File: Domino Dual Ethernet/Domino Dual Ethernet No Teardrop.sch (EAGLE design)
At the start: 37 parts, among them J1 HL-59T-2X1, J2 MH18-1, J3 MH18-1

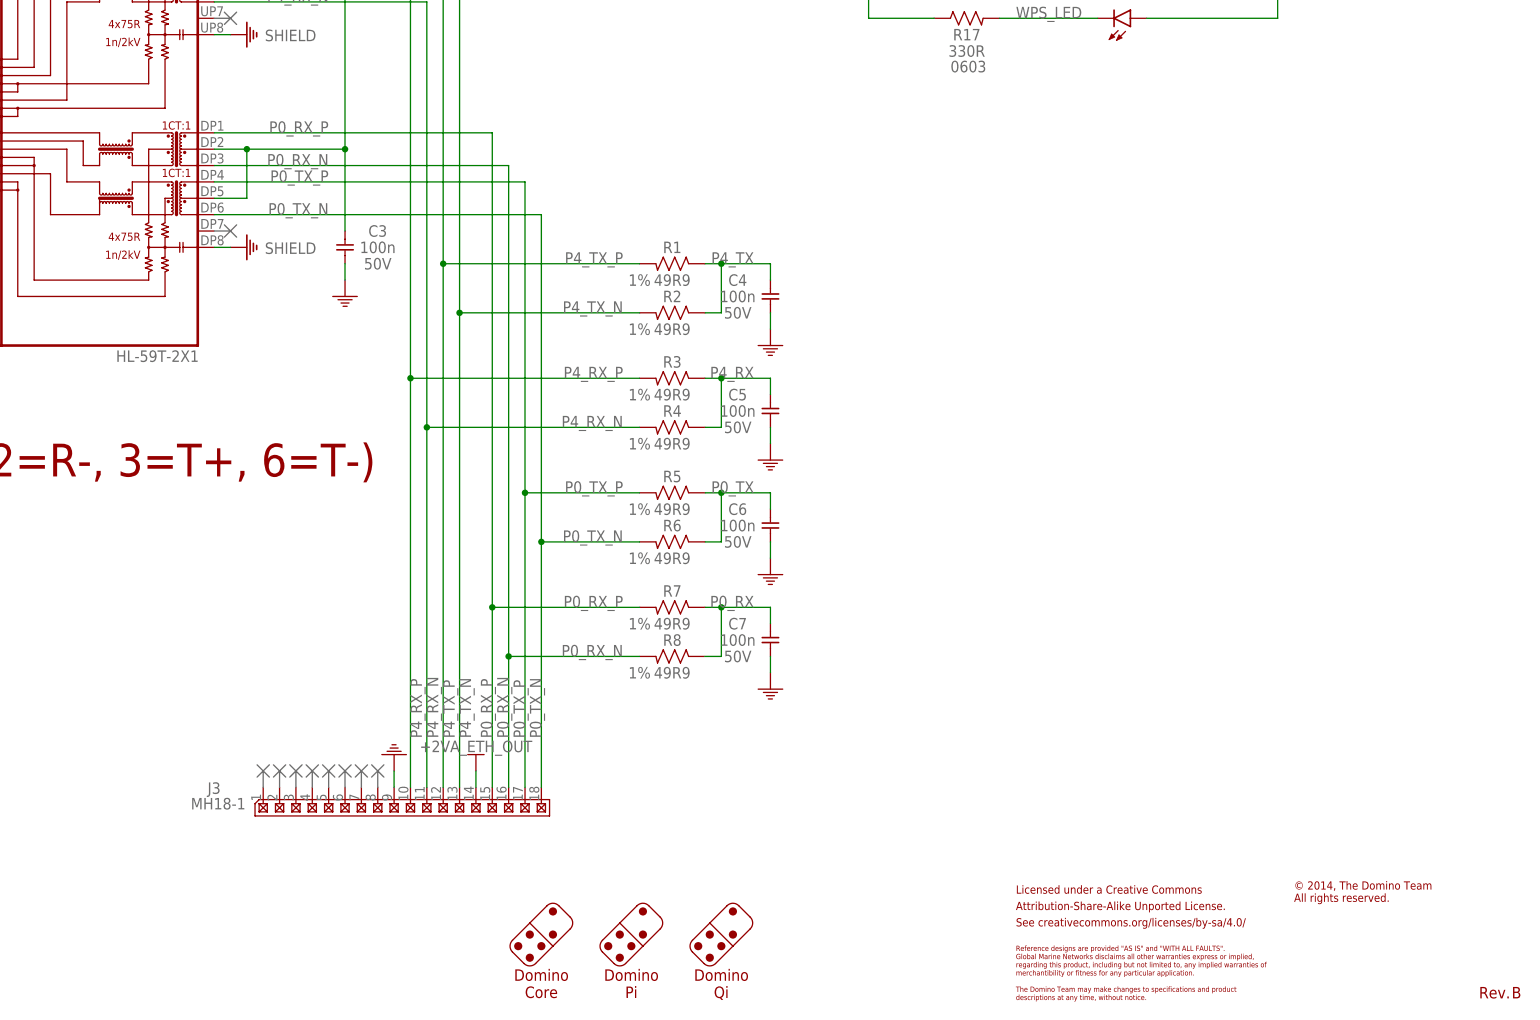
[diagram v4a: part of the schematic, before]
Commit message: Domino Dual Ethernet Rev. C: Changed dual Magjack connector for new one, changed Logos
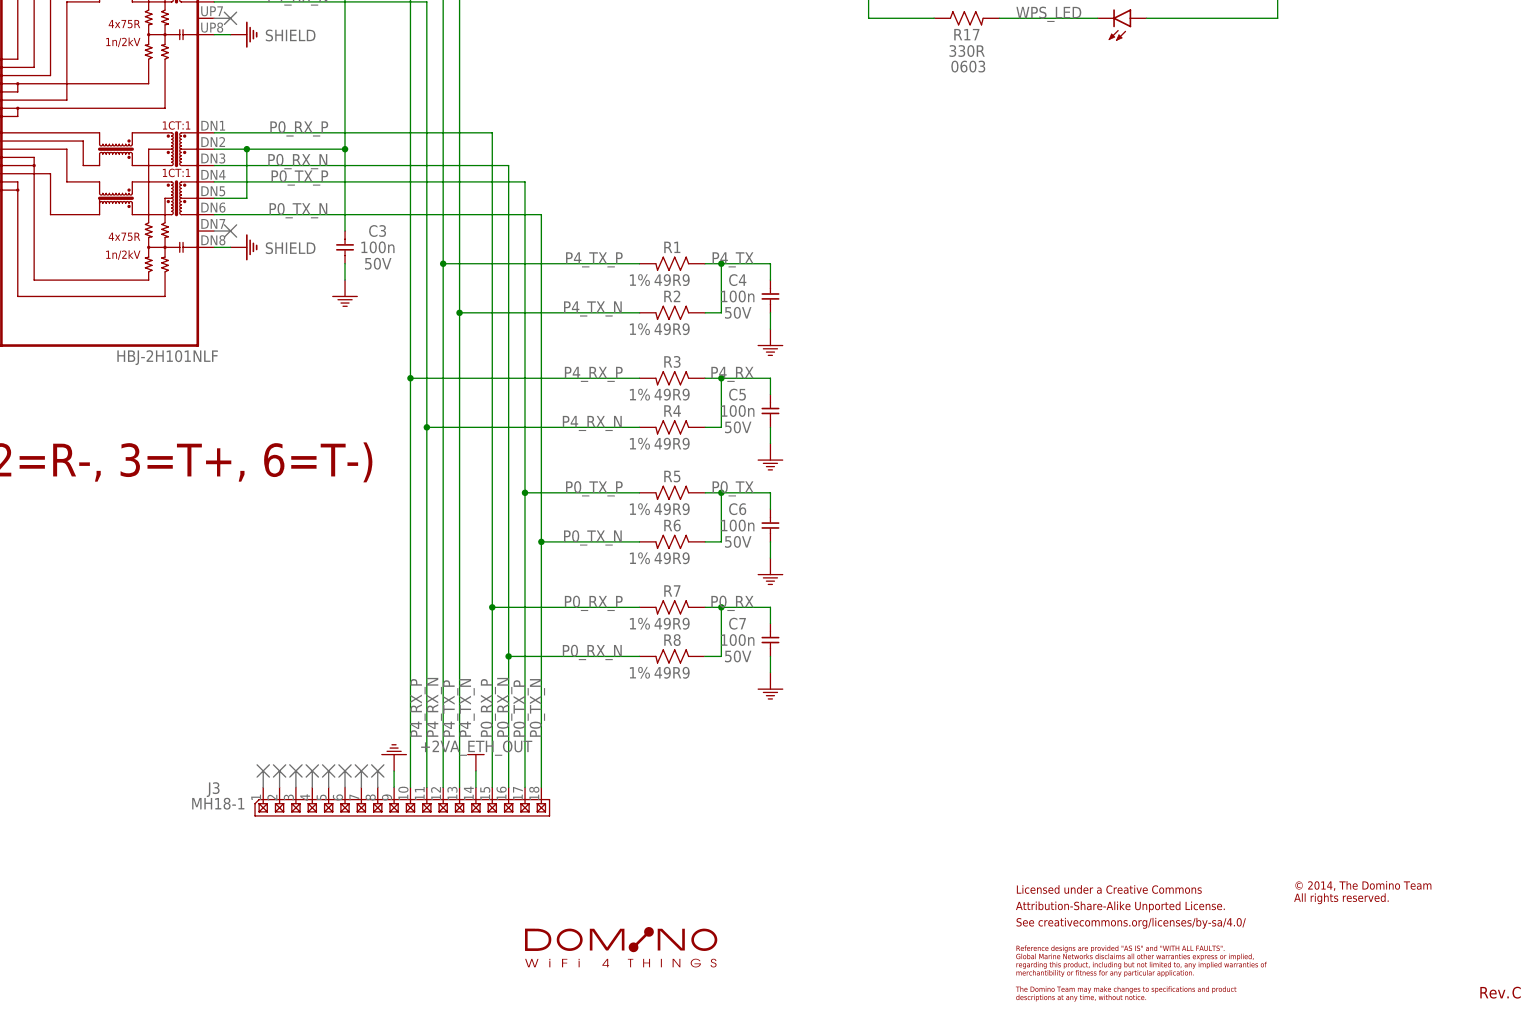
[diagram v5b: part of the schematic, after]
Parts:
- added U$10: DOMINO_LOGO, Domino:DOMINO_LOGO
- J1: value HL-59T-2X1 -> HBJ-2H101NLF; device Domino:HL-59T-2X1 -> Domino:HBJ-2H101NLF; PARTNO HL-59T-2X1 -> HBJ-2H101NLF
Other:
- note removed: "Domino Core"
- note removed: "Domino Pi"
- note removed: "Domino Qi"
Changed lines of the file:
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@@
 <layer number="54" name="bGND_GNDA" color="1" fill="9" visible="no" active="no"/>
 <layer number="56" name="wert" color="7" fill="1" visible="no" active="no"/>
+<layer number="90" name="Modules" color="5" fill="1" visible="yes" active="yes"/>
 <layer number="91" name="Nets" color="2" fill="1" visible="yes" active="yes"/>
 <layer number="92" name="Busses" color="1" fill="1" visible="yes" active="yes"/>
@@
 <layer number="143" name="mvRestrict" color="7" fill="1" visible="no" active="no"/>
 <layer number="144" name="Drill_legend" color="7" fill="1" visible="yes" active="yes"/>
+<layer number="145" name="DrillLegend_01-16" color="2" fill="9" visible="yes" active="yes"/>
+<layer number="146" name="DrillLegend_01-20" color="3" fill="9" visible="yes" active="yes"/>
 <layer number="147" name="Measures_X8" color="7" fill="1" visible="yes" active="yes"/>
 <layer number="148" name="mDocument" color="7" fill="1" visible="no" active="no"/>
 <layer number="149" name="mReference" color="7" fill="1" visible="no" active="no"/>
+<layer number="150" name="Pinout" color="7" fill="1" visible="yes" active="yes"/>
 <layer number="151" name="HeatSink" color="7" fill="1" visible="yes" active="yes"/>
 <layer number="152" name="mbDocu" color="7" fill="1" visible="no" active="no"/>
@@
 <attribute name="DATABASE" value="./../Common/BOM/Domino_DB.txt"/>
 <attribute name="DRAWN" value="M.STEMPIN"/>
-<attribute name="REV" value="B"/>
+<attribute name="REV" value="C"/>
 </attributes>
 <variantdefs>
@@
 <part name="SHIELD3" library="Domino" deviceset="SHIELD" device=""/>
 <part name="SUPPLY5" library="Domino" deviceset="GND" device=""/>
-<part name="J1" library="Domino" deviceset="HL-59T-2X1" device="">
-<attribute name="PARTNO" value="HL-59T-2X1"/>
-</part>
+<part name="J1" library="Domino" deviceset="HBJ-2H101NLF" device="">
+<attribute name="PARTNO" value="HBJ-2H101NLF"/>
+</part>
+<part name="U$10" library="Domino" deviceset="DOMINO_LOGO" device=""/>
 </parts>
 <sheets>
@@
 <text x="302.26" y="8.89" size="0.8128" layer="94">merchantibility or fitness for any particular application.</text>
 <text x="302.26" y="5.08" size="0.8128" layer="94">descriptions at any time, without notice.</text>
-<wire x1="238.079875" y1="14.341975" x2="240.77395" y2="17.036053125" width="0.1016" layer="94"/>
-<wire x1="240.77395" y1="17.036053125" x2="243.468028125" y2="19.730128125" width="0.1016" layer="94"/>
-<wire x1="243.468028125" y1="19.730128125" x2="245.264078125" y2="19.730128125" width="0.1016" layer="94" curve="-90"/>
-<wire x1="245.264078125" y1="19.730128125" x2="247.060128125" y2="17.934078125" width="0.1016" layer="94"/>
-<wire x1="247.060128125" y1="17.934078125" x2="247.060128125" y2="16.138028125" width="0.1016" layer="94" curve="-90"/>
-<wire x1="247.060128125" y1="16.138028125" x2="244.366053125" y2="13.44395" width="0.1016" layer="94"/>
-<wire x1="244.366053125" y1="13.44395" x2="241.671975" y2="10.749875" width="0.1016" layer="94"/>
-<wire x1="241.671975" y1="10.749875" x2="239.875925" y2="10.749875" width="0.1016" layer="94" curve="-90"/>
-<wire x1="239.875925" y1="10.749875" x2="238.079875" y2="12.545925" width="0.1016" layer="94"/>
-<wire x1="238.079875" y1="12.545925" x2="238.079875" y2="14.341975" width="0.1016" layer="94" curve="-90"/>
-<wire x1="240.77395" y1="17.036053125" x2="244.366053125" y2="13.44395" width="0.1016" layer="94"/>
-<circle x="238.9779" y="13.44395" radius="0.635" width="0" layer="94"/>
-<circle x="240.77395" y="15.240003125" radius="0.635" width="0" layer="94"/>
-<circle x="240.77395" y="11.6479" radius="0.635" width="0" layer="94"/>
-<circle x="242.57" y="13.44395" radius="0.635" width="0" layer="94"/>
-<circle x="244.366053125" y="15.24" radius="0.635" width="0" layer="94"/>
-<circle x="244.366053125" y="18.832103125" radius="0.635" width="0" layer="94"/>
-<wire x1="224.109875" y1="14.341975" x2="226.80395" y2="17.036053125" width="0.1016" layer="94"/>
-<wire x1="226.80395" y1="17.036053125" x2="229.498028125" y2="19.730128125" width="0.1016" layer="94"/>
-<wire x1="229.498028125" y1="19.730128125" x2="231.294078125" y2="19.730128125" width="0.1016" layer="94" curve="-90"/>
-<wire x1="231.294078125" y1="19.730128125" x2="233.090128125" y2="17.934078125" width="0.1016" layer="94"/>
-<wire x1="233.090128125" y1="17.934078125" x2="233.090128125" y2="16.138028125" width="0.1016" layer="94" curve="-90"/>
-<wire x1="233.090128125" y1="16.138028125" x2="230.396053125" y2="13.44395" width="0.1016" layer="94"/>
-<wire x1="230.396053125" y1="13.44395" x2="227.701975" y2="10.749875" width="0.1016" layer="94"/>
-<wire x1="227.701975" y1="10.749875" x2="225.905925" y2="10.749875" width="0.1016" layer="94" curve="-90"/>
-<wire x1="225.905925" y1="10.749875" x2="224.109875" y2="12.545925" width="0.1016" layer="94"/>
-<wire x1="224.109875" y1="12.545925" x2="224.109875" y2="14.341975" width="0.1016" layer="94" curve="-90"/>
-<wire x1="226.80395" y1="17.036053125" x2="230.396053125" y2="13.44395" width="0.1016" layer="94"/>
-<circle x="225.0079" y="13.44395" radius="0.635" width="0" layer="94"/>
-<circle x="226.80395" y="15.240003125" radius="0.635" width="0" layer="94"/>
-<circle x="226.80395" y="11.6479" radius="0.635" width="0" layer="94"/>
-<circle x="228.6" y="13.44395" radius="0.635" width="0" layer="94"/>
-<circle x="230.396053125" y="15.24" radius="0.635" width="0" layer="94"/>
-<circle x="230.396053125" y="18.832103125" radius="0.635" width="0" layer="94"/>
-<wire x1="252.049875" y1="14.341975" x2="254.74395" y2="17.036053125" width="0.1016" layer="94"/>
-<wire x1="254.74395" y1="17.036053125" x2="257.438028125" y2="19.730128125" width="0.1016" layer="94"/>
-<wire x1="257.438028125" y1="19.730128125" x2="259.234078125" y2="19.730128125" width="0.1016" layer="94" curve="-90"/>
-<wire x1="259.234078125" y1="19.730128125" x2="261.030128125" y2="17.934078125" width="0.1016" layer="94"/>
-<wire x1="261.030128125" y1="17.934078125" x2="261.030128125" y2="16.138028125" width="0.1016" layer="94" curve="-90"/>
-<wire x1="261.030128125" y1="16.138028125" x2="258.336053125" y2="13.44395" width="0.1016" layer="94"/>
-<wire x1="258.336053125" y1="13.44395" x2="255.641975" y2="10.749875" width="0.1016" layer="94"/>
-<wire x1="255.641975" y1="10.749875" x2="253.845925" y2="10.749875" width="0.1016" layer="94" curve="-90"/>
-<wire x1="253.845925" y1="10.749875" x2="252.049875" y2="12.545925" width="0.1016" layer="94"/>
-<wire x1="252.049875" y1="12.545925" x2="252.049875" y2="14.341975" width="0.1016" layer="94" curve="-90"/>
-<wire x1="254.74395" y1="17.036053125" x2="258.336053125" y2="13.44395" width="0.1016" layer="94"/>
-<circle x="252.9479" y="13.44395" radius="0.635" width="0" layer="94"/>
-<circle x="254.74395" y="15.240003125" radius="0.635" width="0" layer="94"/>
-<circle x="254.74395" y="11.6479" radius="0.635" width="0" layer="94"/>
-<circle x="256.54" y="13.44395" radius="0.635" width="0" layer="94"/>
-<circle x="258.336053125" y="15.24" radius="0.635" width="0" layer="94"/>
-<circle x="258.336053125" y="18.832103125" radius="0.635" width="0" layer="94"/>
-<text x="228.6" y="7.62" size="1.778" layer="94" align="center">Domino
-Core</text>
-<text x="242.57" y="7.62" size="1.778" layer="94" align="center">Domino
-Pi</text>
-<text x="256.54" y="7.62" size="1.778" layer="94" align="center">Domino
-Qi</text>
 <text x="345.44" y="20.32" size="1.27" layer="94">© 2014, The Domino Team
 All rights reserved.</text>
@@
 <attribute name="PARTNO" x="144.78" y="142.24" size="1.778" layer="96" display="off"/>
 </instance>
+<instance part="U$10" gate="G$1" x="226.06" y="12.7"/>
 </instances>
 <busses>

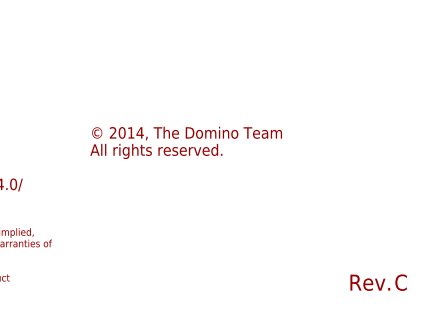
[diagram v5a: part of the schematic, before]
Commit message: Domino Dual Ethernet Rev. D: changed silkscreen font ratio to 20%
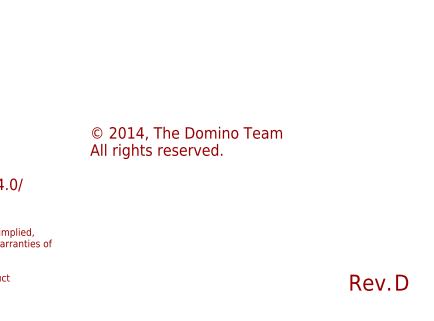
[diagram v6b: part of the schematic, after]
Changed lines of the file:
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@@
 <attribute name="DATABASE" value="./../Common/BOM/Domino_DB.txt"/>
 <attribute name="DRAWN" value="M.STEMPIN"/>
-<attribute name="REV" value="C"/>
+<attribute name="REV" value="D"/>
 </attributes>
 <variantdefs>
